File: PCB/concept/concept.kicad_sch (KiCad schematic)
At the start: 51 parts, among them J1 Antenna, J4 SSD1306 I2C Display, J5 Conn_01x08_Pin, SW1 RotaryEncoder_Switch, U2 Pico

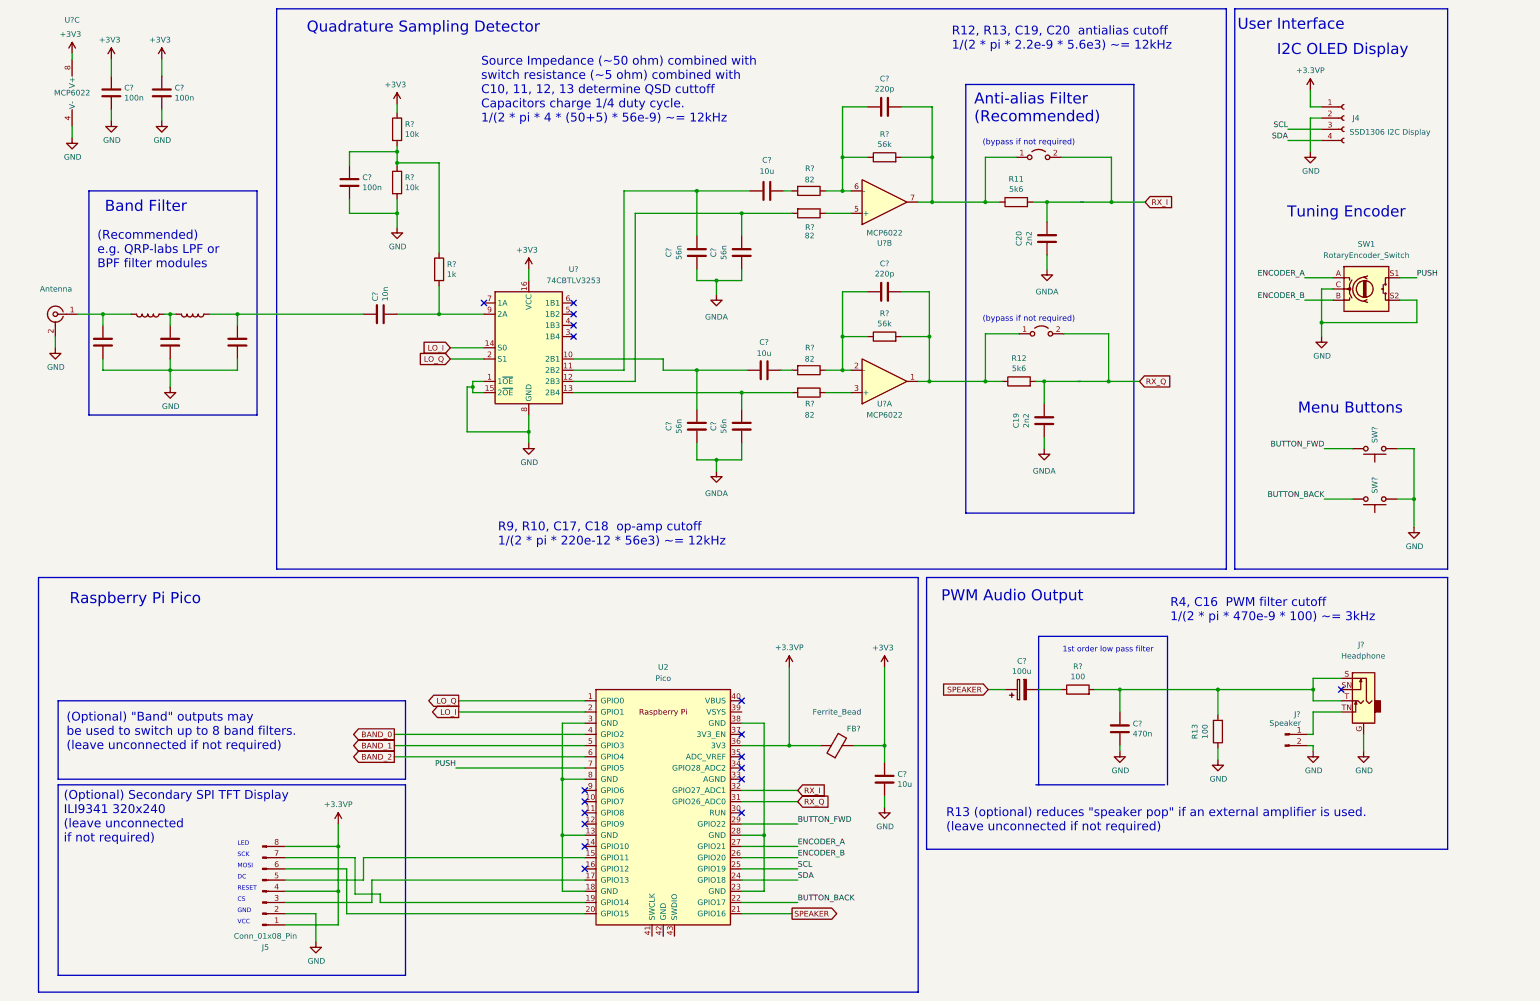
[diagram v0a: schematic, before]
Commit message: Start drawing xcvr concept schemetic
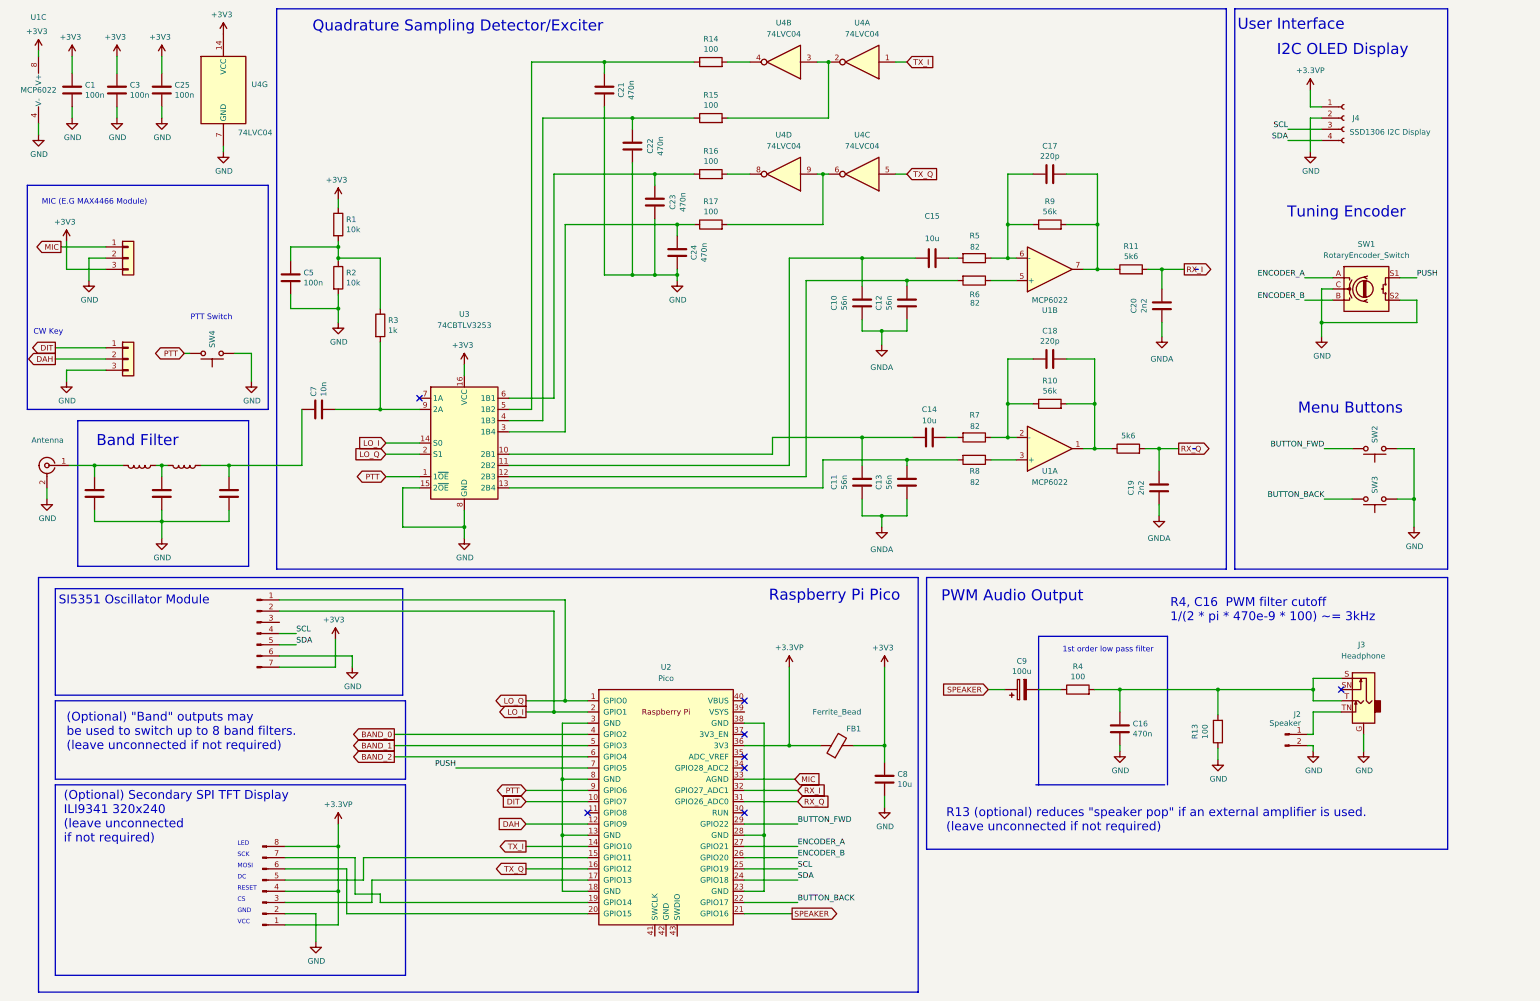
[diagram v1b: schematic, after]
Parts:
- removed JP1, JP2: Jumper_2_Open, symbol Jumper:Jumper_2_Open
- added C21, C22, C23, C24: 470n, Capacitor_SMD:C_0805_2012Metric, symbol Device:C
- added C25: 100n, Capacitor_SMD:C_0805_2012Metric, symbol Device:C
- added J6: Conn_01x07_Pin, symbol Connector:Conn_01x07_Pin
- added J7, J8: Conn_01x03, symbol Connector_Generic:Conn_01x03
- added R14, R15, R16, R17: 100, Resistor_SMD:R_0805_2012Metric, symbol Device:R
- added SW4: SW_Push, Button_Switch_THT:SW_Tactile_SPST_Angled_PTS645Vx31-2LFS, symbol Switch:SW_Push
- added U4: 74LVC04, symbol 74xx:74LS04
- gave numbers to parts that had none: 37
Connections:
- net +3V3: now also C25.1, J6.7 (Pin_7), J7.3 (Pin_3), U4.14 (VCC)
- net GND: now also C21.1, C22.1, C23.1, C24.1, C25.2, J6.6 (Pin_6), J7.2 (Pin_2), J8.3 (Pin_3), SW4.1, U4.7 (GND); no longer U3.1 (1~{OE})
- net LO_I: now also J6.2 (Pin_2)
- net LO_Q: now also J6.1 (Pin_1)
- net SCL: now also J6.4 (Pin_4)
- net SDA: now also J6.5 (Pin_5)
- net DIT: now reaches U2.10 (GPIO7)
- net DIT: now also J8.1 (Pin_1)
- net DAH: now reaches U2.12 (GPIO9)
- net DAH: now also J8.2 (Pin_2)
- net TX_I: now reaches U2.14 (GPIO10)
- net TX_I: now also U4.1
- net TX_Q: now reaches U2.16 (GPIO12)
- net TX_Q: now also U4.5
- net MIC: now reaches U2.33 (AGND)
- net MIC: now also J7.1 (Pin_1)
- net PTT: now reaches U2.9 (GPIO6)
- net PTT: now also U3.1 (1~{OE}), SW4.2
- net at U3.3 (1B4): now also C24.2, R17.1
- net at U3.4 (1B3): now also C22.2, R15.1
- net at U3.5 (1B2): now also C21.2, R14.1
- net at U3.6 (1B1): now also C23.2, R16.1
- new net: R15.2, U4.2, U4.3
- new net: R14.2, U4.4
- new net: R17.2, U4.6, U4.9
- new net: R16.2, U4.8
- no-connect marks 18 -> 8
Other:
- note added: "CW Key"
- note added: "MIC (E.G MAX4466 Module)"
- note added: "PTT Switch"
- note added: "Quadrature Sampling Detector/Exciter"
- note added: "SI5351 Oscillator Module"
- note removed: "(Recommended) e.g. QRP-labs LPF or BPF filter modules"
- note removed: "(bypass if not required)"
- note removed: "Anti-alias Filter (Recommended)"
- note removed: "Quadrature Sampling Detector"
- note removed: "R12, R13, C19, C20 antialias cutoff 1/(2 * pi * 2.2e-9 * 5.6e3) ~= 12kHz"
- note removed: "R9, R10, C17, C18 op-amp cutoff 1/(2 * pi * 220e-12 * 56e3) ~= 12kHz"
- note removed: "Source Impedance (~50 ohm) combined with switch resistance (~5 ohm) combined with C10, 11, 12, 13 determine QSD cuttoff Capacitors charge 1/4 duty cycle. 1/(2 * pi * 4 * (50+5) * 56e-9) ~= 12kHz"
- moved on the sheet: C1, C10, C11, C12, C13, C14, C15, C17, C18, C19, C20, C3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
